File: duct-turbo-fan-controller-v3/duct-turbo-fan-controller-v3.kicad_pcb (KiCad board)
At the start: 2 copper layers, 42.7 x 48.8 mm, 30 parts, among them J1 Screw_Terminal_01x04, J2 Conn_01x04, J3 USB_OTG, J4 AudioJack4, J7 Conn_01x04, Q1 MMBT3904, Q2 BSS84, SW1 SW_Push, SW2 SW_Push, U2 BME680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

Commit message: Fix missing ground on bme68x
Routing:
- net GND: track 37.5 -> 43.9 mm, vias 4 -> 5
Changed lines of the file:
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@@
 			(net 0)
 			(net_name "")
-			(layers "*.Cu")
+			(layers "F&B.Cu")
 			(hatch full 0.508)
 			(connect_pads
@@
 		(tags "resistor handsolder")
 		(property "Reference" "R11"
-			(at 0 1.43 360)
+			(at 0 1.43 0)
 			(layer "B.SilkS")
 			(effects
@@
 		)
 		(property "Value" "4.7k"
-			(at 0 -1.43 360)
+			(at 0 -1.43 0)
 			(layer "B.Fab")
 			(effects
@@
 		)
 		(fp_text user "${REFERENCE}"
-			(at 0 0 360)
+			(at 0 0 0)
 			(layer "B.Fab")
 			(effects
@@
 		(tags "resistor handsolder")
 		(property "Reference" "R10"
-			(at 0 1.43 360)
+			(at 0 1.43 0)
 			(layer "B.SilkS")
 			(effects
@@
 		)
 		(property "Value" "4.7k"
-			(at 0 -1.43 360)
+			(at 0 -1.43 0)
 			(layer "B.Fab")
 			(effects
@@
 		)
 		(fp_text user "${REFERENCE}"
-			(at 0 0 360)
+			(at 0 0 0)
 			(layer "B.Fab")
 			(effects
@@
 	)
 	(segment
+		(start 110.225 80.875)
+		(end 110.225 81.025)
+		(width 0.25)
+		(layer "F.Cu")
+		(net 2)
+	)
+	(segment
 		(start 111.55 90.7)
 		(end 111.7 90.85)
@@
 	)
 	(segment
+		(start 109.475 81.775)
+		(end 109.475 83.5)
+		(width 0.25)
+		(layer "F.Cu")
+		(net 2)
+	)
+	(segment
 		(start 109.6 91.65)
 		(end 109.325 91.65)
@@
 	)
 	(segment
+		(start 110.225 81.025)
+		(end 109.475 81.775)
+		(width 0.25)
+		(layer "F.Cu")
+		(net 2)
+	)
+	(segment
 		(start 111.437501 89.25)
 		(end 111.7 89.25)
@@
 	)
 	(via
+		(at 110.225 80.875)
+		(size 0.8)
+		(drill 0.4)
+		(layers "F.Cu" "B.Cu")
+		(net 2)
+	)
+	(via
 		(at 104.45 83.175)
 		(size 0.8)
@@
 	)
 	(segment
+		(start 112.6 83.275)
+		(end 110.225 80.9)
+		(width 0.25)
+		(layer "B.Cu")
+		(net 2)
+	)
+	(segment
 		(start 100.0049 91.05)
 		(end 100.725 91.05)
 		(width 0.25)
 		(layer "B.Cu")
+		(net 2)
+	)
+	(segment
+		(start 110.225 80.9)
+		(end 110.225 80.875)
+		(width 0.25)
+		(layer "B.Cu")

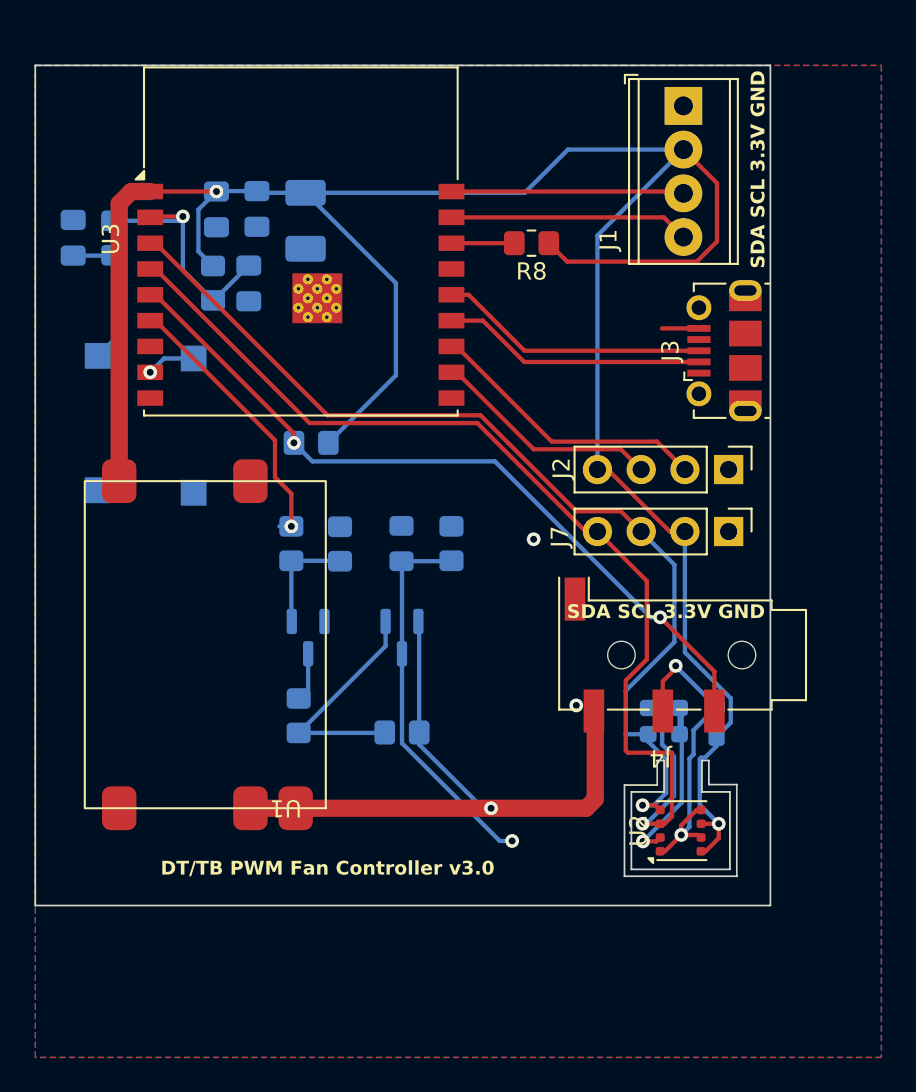
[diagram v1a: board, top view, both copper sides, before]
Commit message: Add diode from usb 5v to power in.
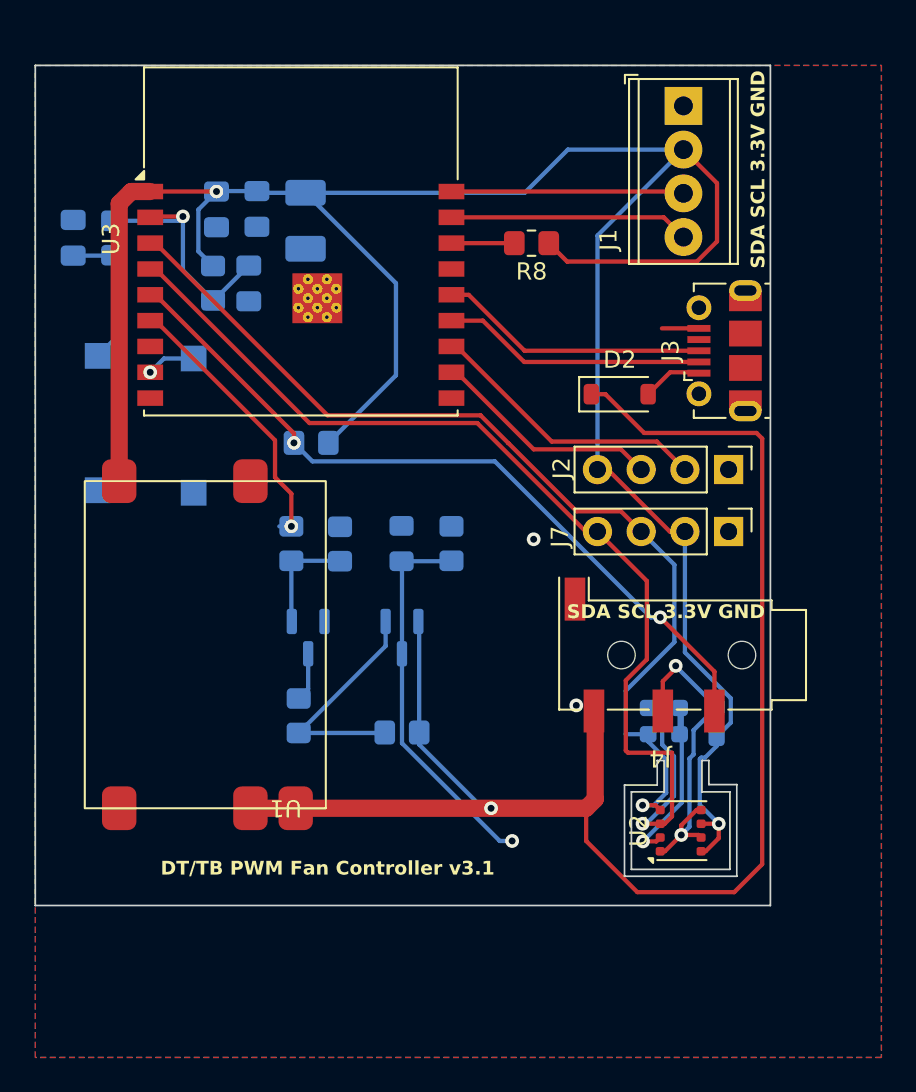
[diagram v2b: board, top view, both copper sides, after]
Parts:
- added D2: D_Small, Diode_SMD:D_SOD-123, F.Cu at (107.0, 65.1)
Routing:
- net +10V: track 38.3 -> 88.0 mm
- net +5V: track 0.00 -> 3.50 mm
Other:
- board text added: "DT/TB PWM Fan Controller v3.1"
- board text removed: "DT/TB PWM Fan Controller v3.0"

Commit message: Bump version for next release
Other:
- board text added: "DT/TB PWM Fan Controller v3.2"
- board text removed: "DT/TB PWM Fan Controller v3.1"
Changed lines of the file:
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@@
 		(layer "Edge.Cuts")
 	)
-	(gr_text "DT/TB PWM Fan Controller v3.1"
+	(gr_text "DT/TB PWM Fan Controller v3.2"
 		(at 80.3 93.1 0)
 		(layer "F.SilkS")
